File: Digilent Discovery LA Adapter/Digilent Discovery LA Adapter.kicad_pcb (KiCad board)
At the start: 2 copper layers, 32.5 x 62.9 mm, 6 parts, among them J1 Cerberus_Expansion, J2 Card_Header, J3 LA_Header, J4 XE_Header

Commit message: labeled DD headers in sch and updated to pcb
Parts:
- removed the J3 at (162.6, 66.0)
- added J4: Addr_Data, Connector_PinSocket_2.54mm:PinSocket_2x16_P2.54mm_Vertical, F.Cu at (122.2, 70.5)
- added J5: CTRL2, Connector_PinSocket_2.54mm:PinSocket_2x05_P2.54mm_Vertical, F.Cu at (129.3, 70.5)
- added J6: XE_LA, Connector_PinHeader_2.54mm:PinHeader_1x02_P2.54mm_Vertical, F.Cu at (126.8, 85.2)
- added J7: Power, Connector_PinHeader_2.54mm:PinHeader_1x02_P2.54mm_Vertical, F.Cu at (131.4, 85.2)
- moved J2 25.4 mm to (162.6, 66.0)
- renumbered J4 to J3
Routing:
- net +5V: track 39.2 -> 0.00 mm
- net /XIN: track 27.9 -> 13.9 mm
- net /XA0: track 27.5 -> 13.8 mm
- net /XD7: track 27.4 -> 13.7 mm
- net /XD2: track 27.5 -> 13.7 mm
- net /XA4: track 27.4 -> 13.7 mm
- net /XSLC: track 27.4 -> 13.7 mm
- net /XBUSACK: track 27.5 -> 13.8 mm
- net /XA9: track 27.4 -> 13.7 mm
- net /XA14: track 27.5 -> 13.8 mm
- net /XA13: track 27.4 -> 13.7 mm
- net /XE: track 50.9 -> 37.1 mm
- net /XD3: track 27.5 -> 13.7 mm
- net /XRD: track 27.5 -> 13.7 mm
- net /XD1: track 27.5 -> 13.8 mm
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
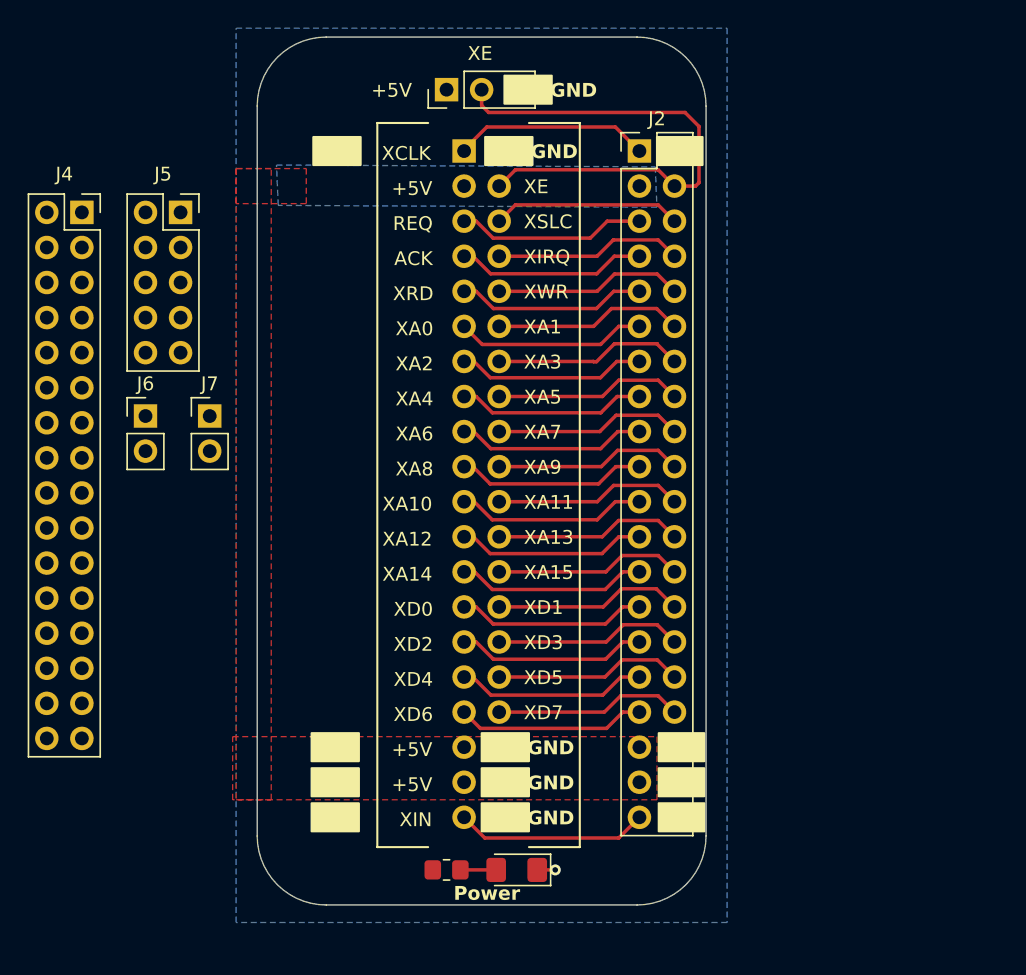
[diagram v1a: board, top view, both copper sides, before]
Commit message: thermal drc "error"
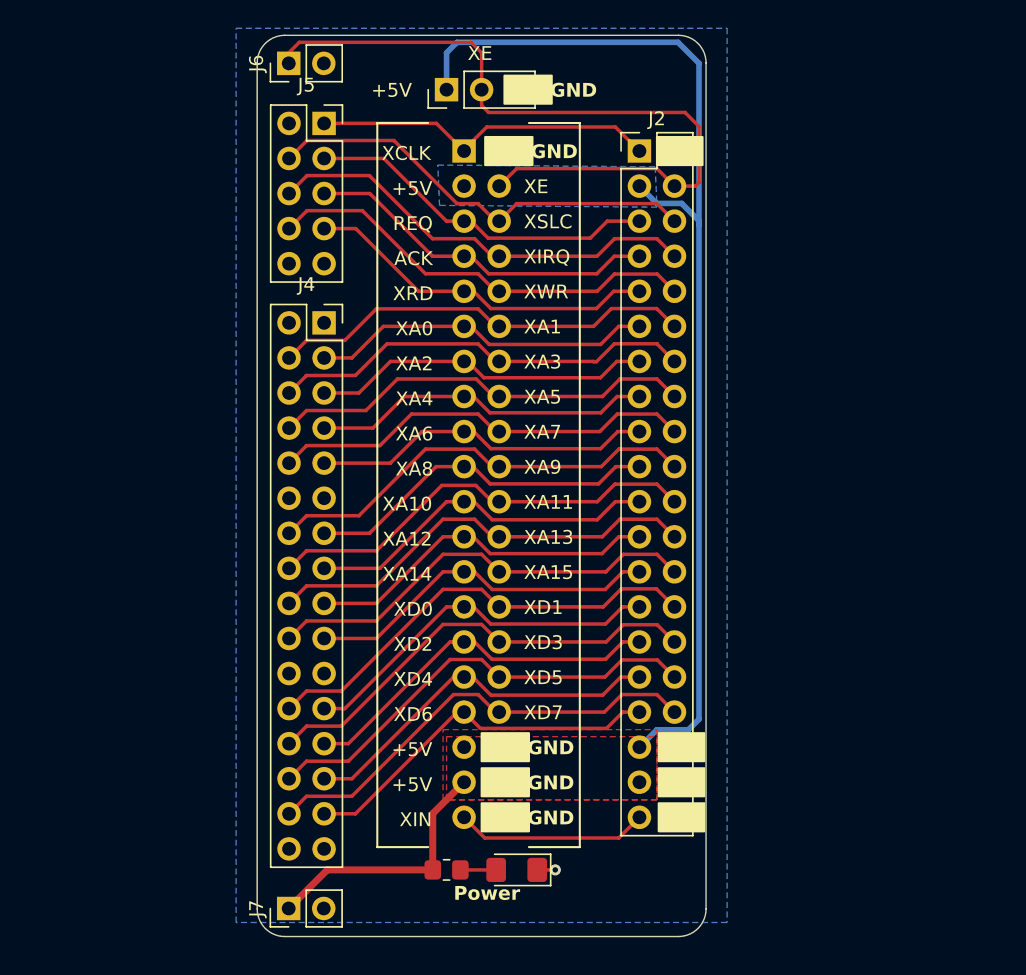
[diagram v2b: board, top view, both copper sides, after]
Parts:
- moved J7 36.1 mm to (137.2, 120.9), turned to 90 degrees
- moved J6 27.6 mm to (137.2, 59.7), turned to 90 degrees
- moved J4 19.3 mm to (139.7, 78.5)
- moved J5 12.2 mm to (139.7, 64.0)
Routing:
- net +5V: track 0.00 -> 99.1 mm
- net /XD7: track 13.7 -> 33.1 mm
- net /XD5: track 13.7 -> 33.1 mm
- net /XD1: track 13.8 -> 33.1 mm
- net /XD3: track 13.7 -> 33.1 mm
- net /XA9: track 13.7 -> 32.0 mm
- net /XA13: track 13.7 -> 32.0 mm
- net /XA15: track 13.7 -> 32.0 mm
- net /XA11: track 13.7 -> 31.9 mm
- net /XSLC: track 13.7 -> 31.9 mm
- net /XIRQ: track 13.7 -> 31.9 mm
- net /XWR: track 13.7 -> 31.9 mm
- net /XE: track 37.1 -> 55.3 mm
- net /XA7: track 13.7 -> 31.0 mm
- net /XA5: track 13.7 -> 31.0 mm
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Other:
- board size 32.5 x 62.9 mm -> 32.5 x 65.3 mm
- board text added: "cerberus 2100 DD LA adapter rev1, @baldengineer"
- board text removed: "cerberus 2100 1:1 LA adapter rev1, @baldengineer"

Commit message: about to delete extra silk
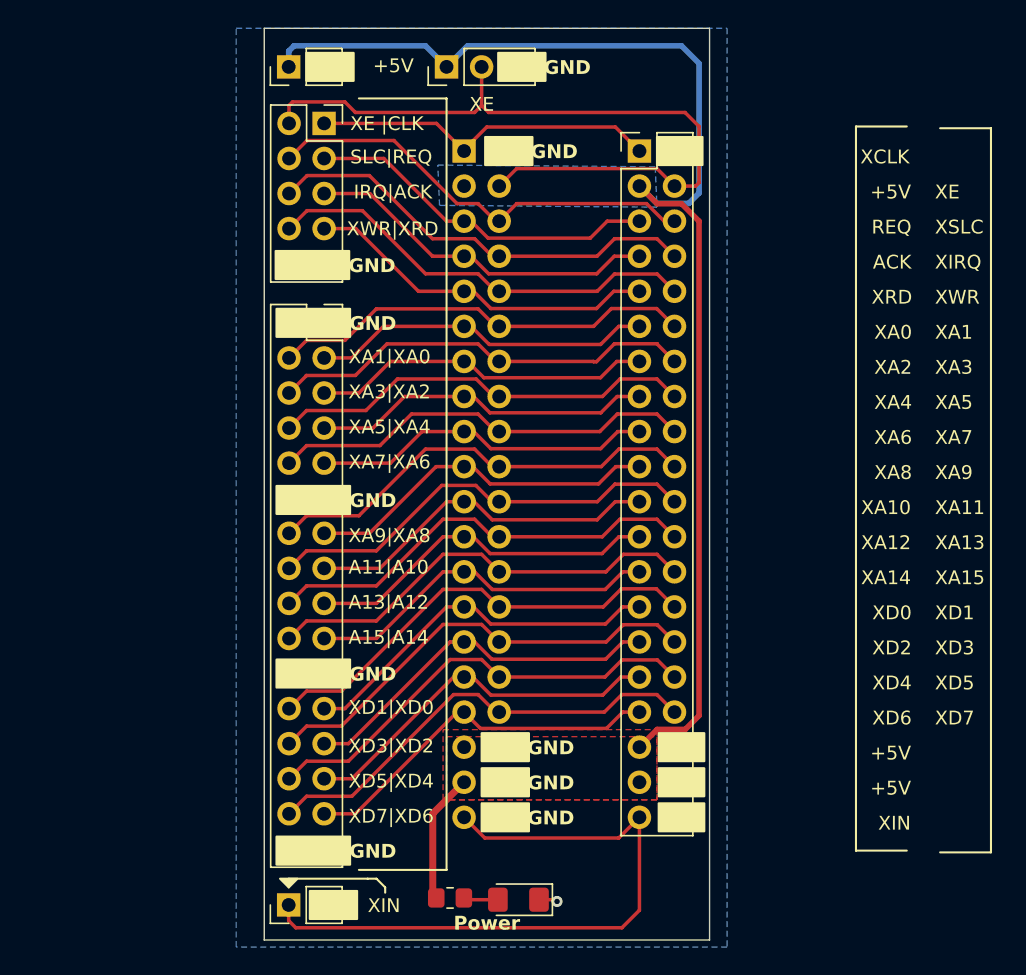
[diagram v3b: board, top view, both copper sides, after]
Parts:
- J6: value XE_LA -> XIN_LA
- moved J6 61.0 mm to (137.2, 120.7)
- moved J7 61.0 mm to (137.2, 59.9)
- moved D1 2.16 mm to (153.8, 120.3)
- moved R1 2.05 mm to (148.8, 120.1)
- moved J3 1.65 mm to (148.6, 59.9)
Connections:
- J5 pad 2: /XIN -> /XE
- J6 pad 1: /XE -> /XIN
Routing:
- net /XIN: track 13.9 -> 48.0 mm
- net +5V: track 99.1 -> 103.2 mm
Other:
- board size 32.5 x 65.3 mm -> 32.3 x 66 mm
- board text added: "A11|A10"
- board text added: "A13|A12"
- board text added: "A15|A14"
- board text added: "IRQ|ACK"
- board text added: "SLC|REQ"
- board text added: "XA1|XA0"
- board text added: "XA3|XA2"
- board text added: "XA5|XA4"
- board text added: "XA7|XA6"
- board text added: "XA9|XA8"
- board text added: "XD1|XD0"
- board text added: "XD3|XD2"
- board text added: "XD5|XD4"
- board text added: "XD7|XD6"
- board text added: "XE |CLK"
- board text added: "XWR|XRD"

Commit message: dd adapter rev 1 ready to go to the fab
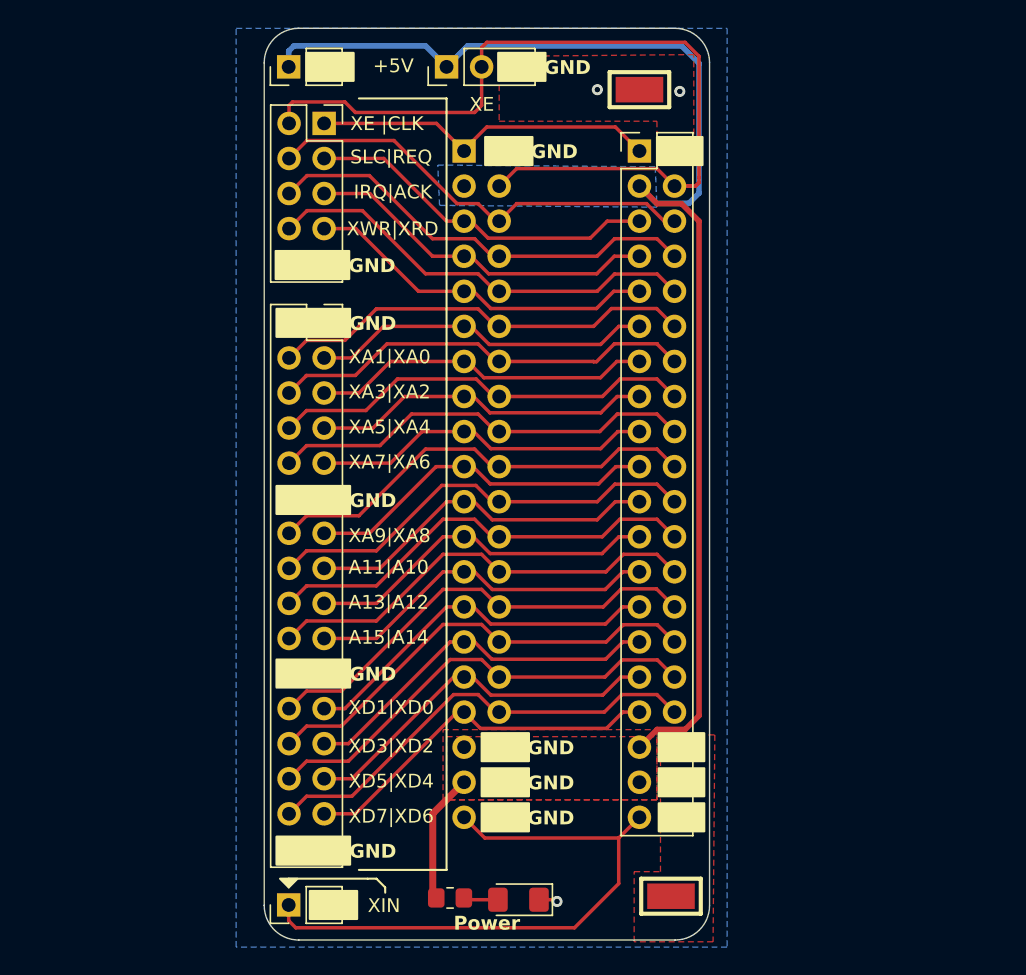
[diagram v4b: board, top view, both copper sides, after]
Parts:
- added TP1: TestPoint_Harwin, My Libraries:Harwin-S1751-46-Test-Point, F.Cu at (164.8, 120.0)
- added TP2: TestPoint_Harwin, My Libraries:Harwin-S1751-46-Test-Point, F.Cu at (162.6, 61.6)
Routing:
- net /XE: track 54.8 -> 63.1 mm
- net /XIN: track 48.0 -> 43.8 mm
- net GND: vias 1 -> 3
- added copper zone on F.Cu, net GND
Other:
- outline, holes or cut-outs redrawn
- board text removed: "ACK"
- board text removed: "REQ"
- board text removed: "XA0"
- board text removed: "XA1"
- board text removed: "XA10"
- board text removed: "XA11"
- board text removed: "XA12"
- board text removed: "XA13"
- board text removed: "XA14"
- board text removed: "XA15"
- board text removed: "XA2"
- board text removed: "XA3"
- board text removed: "XA4"
- board text removed: "XA5"
- board text removed: "XA6"
- board text removed: "XA7"
- board text removed: "XA8"
- board text removed: "XA9"
- board text removed: "XCLK"
- board text removed: "XD0"
- board text removed: "XD1"
- board text removed: "XD2"
- board text removed: "XD3"
- board text removed: "XD4"
- board text removed: "XD5"
- board text removed: "XD6"
- board text removed: "XD7"
- board text removed: "XIRQ"
- board text removed: "XRD"
- board text removed: "XSLC"
- board text removed: "XWR"
